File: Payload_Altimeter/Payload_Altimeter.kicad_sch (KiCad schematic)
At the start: 0 parts

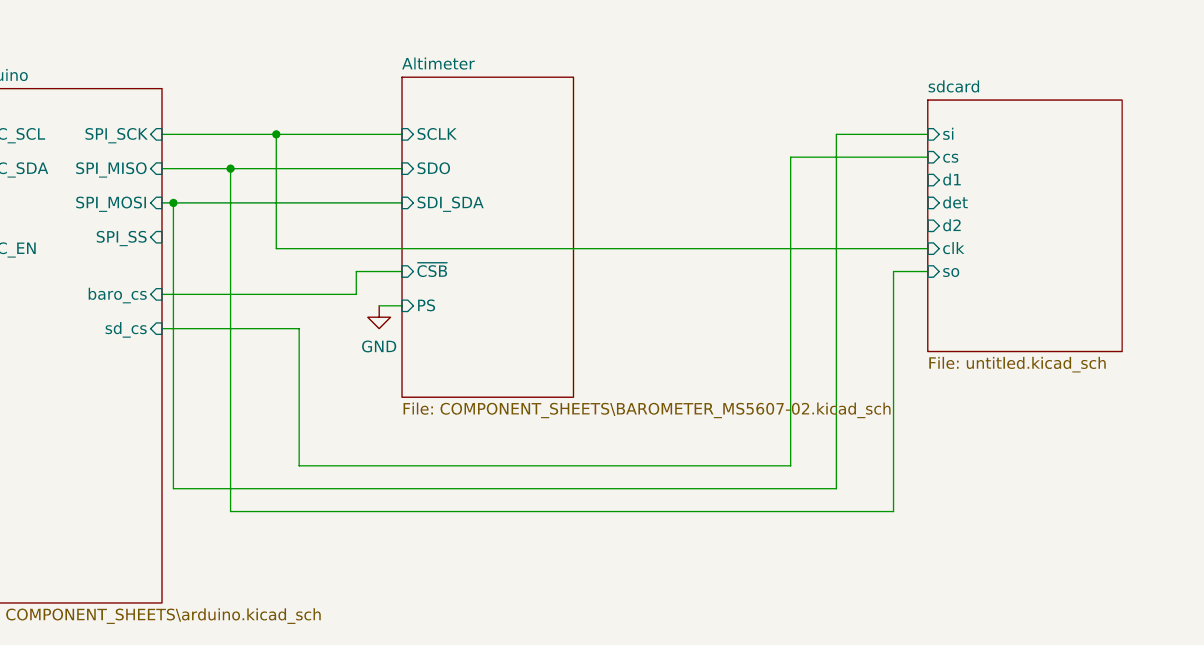
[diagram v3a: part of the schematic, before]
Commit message: SD Card
Got rid of SD card
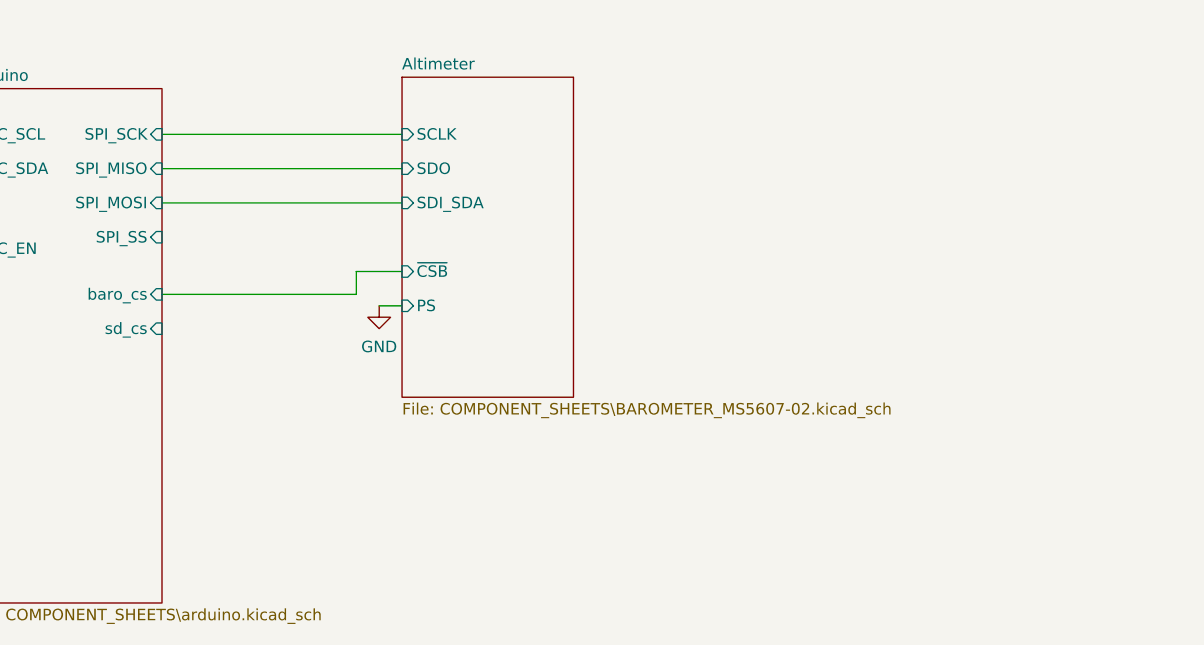
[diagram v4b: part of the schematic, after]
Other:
- removed sheet sdcard
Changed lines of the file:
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@@
 (kicad_sch (version 20211123) (generator eeschema)
   (paper "A4")
-  (junction (at 134.62 71.12) (diameter 0) (color 0 0 0 0)
-  )
-  (junction (at 129.54 74.93) (diameter 0) (color 0 0 0 0)
-  )
-  (junction (at 123.19 78.74) (diameter 0) (color 0 0 0 0)
-  )
-  (wire (pts (xy 134.62 71.12) (xy 148.59 71.12))
-    (stroke (width 0) (type default) (color 0 0 0 0))
-  )
   (wire (pts (xy 66.04 71.12) (xy 100.33 71.12))
     (stroke (width 0) (type default) (color 0 0 0 0))
   )
-  (wire (pts (xy 191.77 107.95) (xy 191.77 73.66))
-    (stroke (width 0) (type default) (color 0 0 0 0))
-  )
-  (wire (pts (xy 196.85 110.49) (xy 196.85 71.12))
-    (stroke (width 0) (type default) (color 0 0 0 0))
-  )
   (wire (pts (xy 143.51 86.36) (xy 148.59 86.36))
     (stroke (width 0) (type default) (color 0 0 0 0))
   )
-  (wire (pts (xy 134.62 83.82) (xy 134.62 71.12))
-    (stroke (width 0) (type default) (color 0 0 0 0))
-  )
-  (wire (pts (xy 123.19 110.49) (xy 196.85 110.49))
-    (stroke (width 0) (type default) (color 0 0 0 0))
-  )
-  (wire (pts (xy 123.19 78.74) (xy 123.19 110.49))
-    (stroke (width 0) (type default) (color 0 0 0 0))
-  )
   (wire (pts (xy 121.92 88.9) (xy 143.51 88.9))
     (stroke (width 0) (type default) (color 0 0 0 0))
   )
-  (wire (pts (xy 129.54 74.93) (xy 148.59 74.93))
-    (stroke (width 0) (type default) (color 0 0 0 0))
-  )
-  (wire (pts (xy 207.01 86.36) (xy 203.2 86.36))
-    (stroke (width 0) (type default) (color 0 0 0 0))
-  )
-  (wire (pts (xy 121.92 92.71) (xy 137.16 92.71))
-    (stroke (width 0) (type default) (color 0 0 0 0))
-  )
-  (wire (pts (xy 123.19 78.74) (xy 148.59 78.74))
+  (wire (pts (xy 121.92 78.74) (xy 148.59 78.74))
     (stroke (width 0) (type default) (color 0 0 0 0))
   )
@@
     (stroke (width 0) (type default) (color 0 0 0 0))
   )
-  (wire (pts (xy 196.85 71.12) (xy 207.01 71.12))
-    (stroke (width 0) (type default) (color 0 0 0 0))
-  )
   (wire (pts (xy 143.51 88.9) (xy 143.51 86.36))
     (stroke (width 0) (type default) (color 0 0 0 0))
   )
-  (wire (pts (xy 121.92 78.74) (xy 123.19 78.74))
-    (stroke (width 0) (type default) (color 0 0 0 0))
-  )
-  (wire (pts (xy 203.2 113.03) (xy 129.54 113.03))
-    (stroke (width 0) (type default) (color 0 0 0 0))
-  )
-  (wire (pts (xy 129.54 113.03) (xy 129.54 74.93))
-    (stroke (width 0) (type default) (color 0 0 0 0))
-  )
   (wire (pts (xy 146.05 90.17) (xy 148.59 90.17))
     (stroke (width 0) (type default) (color 0 0 0 0))
   )
-  (wire (pts (xy 137.16 92.71) (xy 137.16 107.95))
-    (stroke (width 0) (type default) (color 0 0 0 0))
-  )
-  (wire (pts (xy 137.16 107.95) (xy 191.77 107.95))
-    (stroke (width 0) (type default) (color 0 0 0 0))
-  )
-  (wire (pts (xy 191.77 73.66) (xy 207.01 73.66))
-    (stroke (width 0) (type default) (color 0 0 0 0))
-  )
-  (wire (pts (xy 207.01 83.82) (xy 134.62 83.82))
-    (stroke (width 0) (type default) (color 0 0 0 0))
-  )
-  (wire (pts (xy 121.92 74.93) (xy 129.54 74.93))
+  (wire (pts (xy 121.92 74.93) (xy 148.59 74.93))
     (stroke (width 0) (type default) (color 0 0 0 0))
   )
@@
     (stroke (width 0) (type default) (color 0 0 0 0))
   )
-  (wire (pts (xy 121.92 71.12) (xy 134.62 71.12))
-    (stroke (width 0) (type default) (color 0 0 0 0))
-  )
-  (wire (pts (xy 203.2 86.36) (xy 203.2 113.03))
+  (wire (pts (xy 121.92 71.12) (xy 148.59 71.12))
     (stroke (width 0) (type default) (color 0 0 0 0))
   )
@@
     )
   )
-  (sheet (at 207.01 67.31) (size 21.59 27.94) (fields_autoplaced)
-    (stroke (width 0.1524) (type solid) (color 0 0 0 0))
-    (fill (color 0 0 0 0.0000))
-    (property "Sheet name" "sdcard" (id 0) (at 207.01 66.5984 0)
-      (effects (font (size 1.27 1.27)) (justify left bottom))
-    )
-    (property "Sheet file" "untitled.kicad_sch" (id 1) (at 207.01 95.8346 0)
-      (effects (font (size 1.27 1.27)) (justify left top))
-    )
-    (pin "si" input (at 207.01 71.12 180)
-      (effects (font (size 1.27 1.27)) (justify left))
-    )
-    (pin "cs" input (at 207.01 73.66 180)
-      (effects (font (size 1.27 1.27)) (justify left))
-    )
-    (pin "d1" input (at 207.01 76.2 180)
-      (effects (font (size 1.27 1.27)) (justify left))
-    )
-    (pin "det" input (at 207.01 78.74 180)
-      (effects (font (size 1.27 1.27)) (justify left))
-    )
-    (pin "d2" input (at 207.01 81.28 180)
-      (effects (font (size 1.27 1.27)) (justify left))
-    )
-    (pin "clk" input (at 207.01 83.82 180)
-      (effects (font (size 1.27 1.27)) (justify left))
-    )
-    (pin "so" input (at 207.01 86.36 180)
-      (effects (font (size 1.27 1.27)) (justify left))
-    )
-  )
   (sheet_instances
     (path "/" (page "1"))
@@
     (path "/5fba5415-62df-4f11-b066-c862c7f4f614" (page "3"))
     (path "/18be7ca6-5942-4bc1-bf13-c4393b1dbad1" (page "4"))
-    (path "/abdb6179-bbd9-4d88-83fc-0a11cdff4490" (page "5"))
   )
   (symbol_instances
@@
       (reference "#PWR0105") (unit 1) (value "+5V") (footprint "")
     )
-    (path "/abdb6179-bbd9-4d88-83fc-0a11cdff4490/b48e6861-adf2-4473-858f-d65f8dcea6c9"
-      (reference "#PWR0106") (unit 1) (value "+3V3") (footprint "")
-    )
-    (path "/abdb6179-bbd9-4d88-83fc-0a11cdff4490/d5954016-c980-4371-a52c-a53007d822f3"
-      (reference "#PWR0107") (unit 1) (value "GND") (footprint "")
-    )
     (path "/5fba5415-62df-4f11-b066-c862c7f4f614/00000000-0000-0000-0000-000061610282"
       (reference "C12") (unit 1) (value "100nF") (footprint "Capacitor_SMD:C_0201_0603Metric")
@@
       (reference "J1") (unit 1) (value "L717SDC37P1ACH4F") (footprint "RDT_Custom_Footprints:L717SDC37P1ACH4F")
     )
-    (path "/abdb6179-bbd9-4d88-83fc-0a11cdff4490/71d6f518-fb46-4753-adea-d4368d3f3e26"
-      (reference "J2") (unit 1) (value "Conn_01x09") (footprint "Connector_PinHeader_2.54mm:PinHeader_1x09_P2.54mm_Vertical")
-    )
     (path "/18be7ca6-5942-4bc1-bf13-c4393b1dbad1/4ac59da2-094a-4712-84ed-13816bdf2b3f"

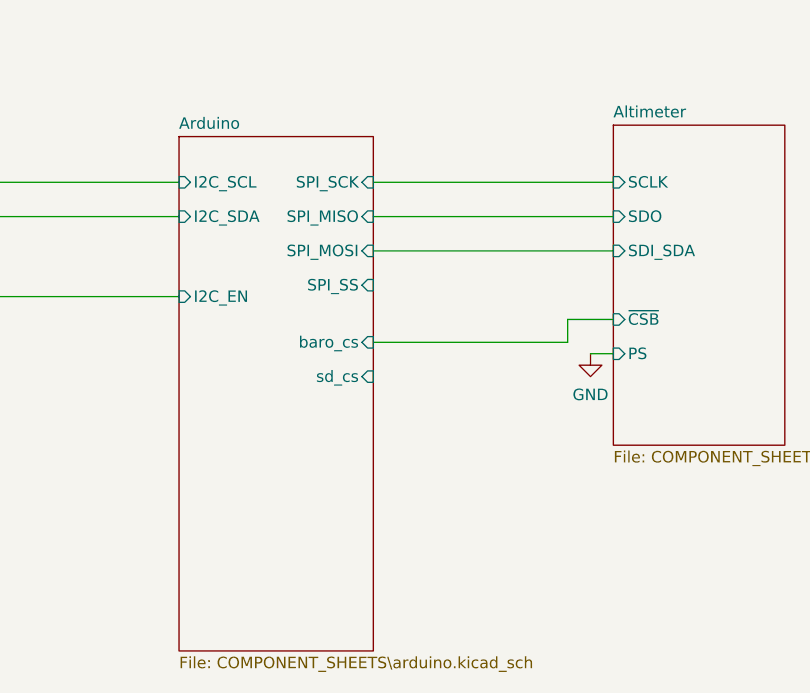
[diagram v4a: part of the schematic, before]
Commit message: Rasp_Pi
Tried to put in a pi zero
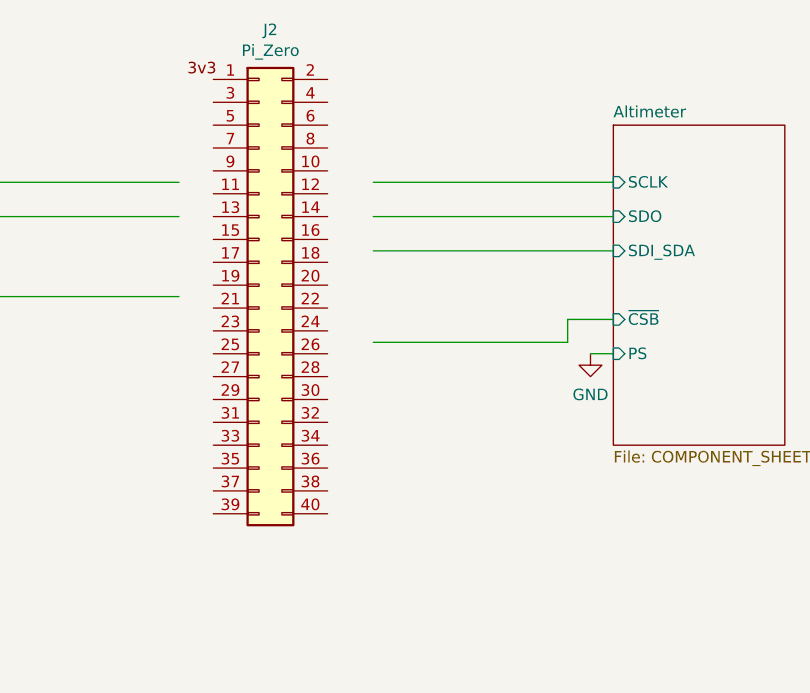
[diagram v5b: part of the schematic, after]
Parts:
- added J2: Pi_Zero, Connector_PinHeader_2.54mm:PinHeader_2x20_P2.54mm_Vertical, symbol Connector_Generic:Conn_02x20_Odd_Even
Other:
- removed sheet Arduino
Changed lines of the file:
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@@
     (stroke (width 0) (type default) (color 0 0 0 0))
+  )
+  (symbol (lib_id "Connector_Generic:Conn_02x20_Odd_Even") (at 109.22 82.55 0) (unit 1)
+    (in_bom yes) (on_board yes)
+    (property "Reference" "J2" (id 0) (at 110.49 54.1782 0))
+    (property "Value" "Pi_Zero" (id 1) (at 110.49 56.4896 0))
+    (property "Footprint" "Connector_PinHeader_2.54mm:PinHeader_2x20_P2.54mm_Vertical" (id 2) (at 109.22 82.55 0)
+      (effects (font (size 1.27 1.27)) hide)
+    )
+    (property "Datasheet" "~" (id 3) (at 109.22 82.55 0)
+      (effects (font (size 1.27 1.27)) hide)
+    )
+    (pin "1")
+    (pin "10")
+    (pin "11")
+    (pin "12")
+    (pin "13")
+    (pin "14")
+    (pin "15")
+    (pin "16")
+    (pin "17")
+    (pin "18")
+    (pin "19")
+    (pin "2")
+    (pin "20")
+    (pin "21")
+    (pin "22")
+    (pin "23")
+    (pin "24")
+    (pin "25")
+    (pin "26")
+    (pin "27")
+    (pin "28")
+    (pin "29")
+    (pin "3")
+    (pin "30")
+    (pin "31")
+    (pin "32")
+    (pin "33")
+    (pin "34")
+    (pin "35")
+    (pin "36")
+    (pin "37")
+    (pin "38")
+    (pin "39")
+    (pin "4")
+    (pin "40")
+    (pin "5")
+    (pin "6")
+    (pin "7")
+    (pin "8")
+    (pin "9")
   )
   (symbol (lib_id "power:GND") (at 146.05 90.17 0) (unit 1)
@@
     )
   )
-  (sheet (at 100.33 66.04) (size 21.59 57.15) (fields_autoplaced)
-    (stroke (width 0.1524) (type solid) (color 0 0 0 0))
-    (fill (color 0 0 0 0.0000))
-    (property "Sheet name" "Arduino" (id 0) (at 100.33 65.3284 0)
-      (effects (font (size 1.27 1.27)) (justify left bottom))
-    )
-    (property "Sheet file" "COMPONENT_SHEETS\\arduino.kicad_sch" (id 1) (at 100.33 123.7746 0)
-      (effects (font (size 1.27 1.27)) (justify left top))
-    )
-    (pin "I2C_SCL" input (at 100.33 71.12 180)
-      (effects (font (size 1.27 1.27)) (justify left))
-    )
-    (pin "I2C_SDA" input (at 100.33 74.93 180)
-      (effects (font (size 1.27 1.27)) (justify left))
-    )
-    (pin "I2C_EN" input (at 100.33 83.82 180)
-      (effects (font (size 1.27 1.27)) (justify left))
-    )
-    (pin "SPI_SCK" input (at 121.92 71.12 0)
-      (effects (font (size 1.27 1.27)) (justify right))
-    )
-    (pin "SPI_MISO" input (at 121.92 74.93 0)
-      (effects (font (size 1.27 1.27)) (justify right))
-    )
-    (pin "SPI_MOSI" input (at 121.92 78.74 0)
-      (effects (font (size 1.27 1.27)) (justify right))
-    )
-    (pin "SPI_SS" input (at 121.92 82.55 0)
-      (effects (font (size 1.27 1.27)) (justify right))
-    )
-    (pin "baro_cs" input (at 121.92 88.9 0)
-      (effects (font (size 1.27 1.27)) (justify right))
-    )
-    (pin "sd_cs" input (at 121.92 92.71 0)
-      (effects (font (size 1.27 1.27)) (justify right))
-    )
-  )
   (sheet (at 148.59 64.77) (size 19.05 35.56) (fields_autoplaced)
     (stroke (width 0.1524) (type solid) (color 0 0 0 0))
@@
     (path "/0730ce47-0bea-44a3-992c-5d03f0a08e83" (page "2"))
     (path "/5fba5415-62df-4f11-b066-c862c7f4f614" (page "3"))
-    (path "/18be7ca6-5942-4bc1-bf13-c4393b1dbad1" (page "4"))
   )
   (symbol_instances
@@
       (reference "#PWR0101") (unit 1) (value "GND") (footprint "")
     )
-    (path "/18be7ca6-5942-4bc1-bf13-c4393b1dbad1/98b5fd41-6856-4d34-bc02-2d1bbe8972be"
-      (reference "#PWR0102") (unit 1) (value "+5V") (footprint "")
-    )
-    (path "/18be7ca6-5942-4bc1-bf13-c4393b1dbad1/44276706-5572-4ca8-88fc-56e6f30954a6"
-      (reference "#PWR0103") (unit 1) (value "GND") (footprint "")
-    )
     (path "/0730ce47-0bea-44a3-992c-5d03f0a08e83/58442b5d-6983-40cc-bc9c-d8f0af4d6d86"
       (reference "#PWR0104") (unit 1) (value "+5V") (footprint "")
@@
       (reference "J1") (unit 1) (value "L717SDC37P1ACH4F") (footprint "RDT_Custom_Footprints:L717SDC37P1ACH4F")
     )
-    (path "/18be7ca6-5942-4bc1-bf13-c4393b1dbad1/4ac59da2-094a-4712-84ed-13816bdf2b3f"
-      (reference "U1") (unit 1) (value "Arduino_Pro_Mini") (footprint "Arduino:Arduino_Pro_Mini")
+    (path "/3c366a71-f7c8-4705-a28c-1a6b708315a6"
+      (reference "J2") (unit 1) (value "Pi_Zero") (footprint "Connector_PinHeader_2.54mm:PinHeader_2x20_P2.54mm_Vertical")
     )
     (path "/5fba5415-62df-4f11-b066-c862c7f4f614/00000000-0000-0000-0000-00006161026e"

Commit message: Finished Schematic?
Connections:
- net Pi_3v3: now reaches J2.1 (3v3)
- net MOSI: now reaches J2.19 (Pin_19)
- net +5V: now reaches J2.2 (Pin_2)
- net +5V: now also J2.4 (Pin_4)
- net MISO: now reaches J2.21 (Pin_21)
- net SCLK: now reaches J2.23 (Pin_23)
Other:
- sheet Altimeter renamed Barometer
- sheet Barometer ports: added 3v3, MISO, MOSI; removed PS, SDI_SDA, SDO, ~{CSB}

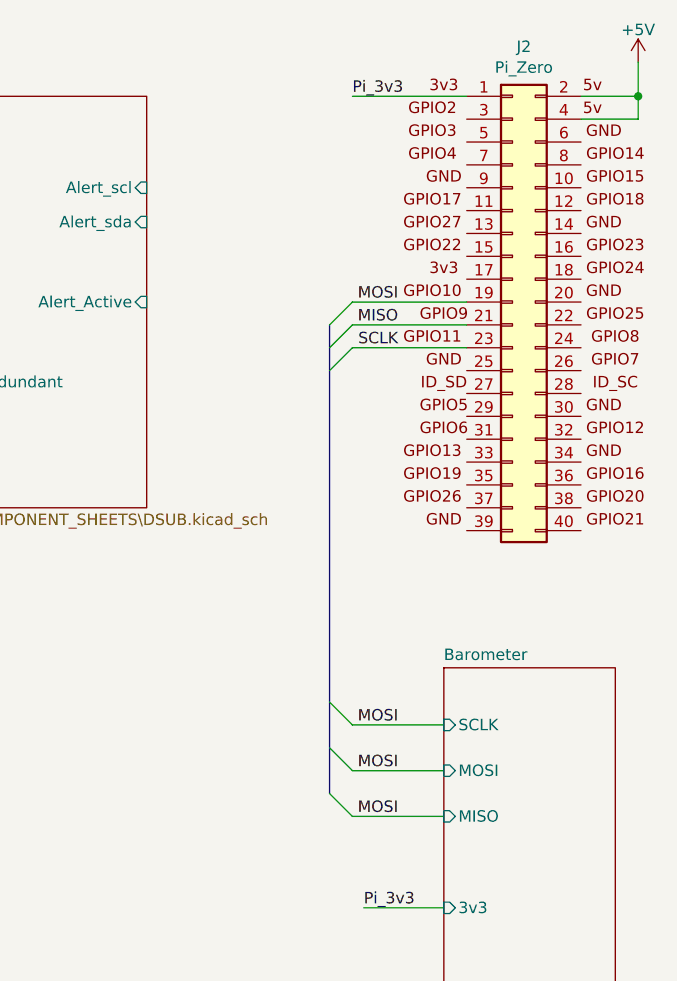
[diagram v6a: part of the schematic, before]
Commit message: Some connection
Put some of the connections on but not all of them
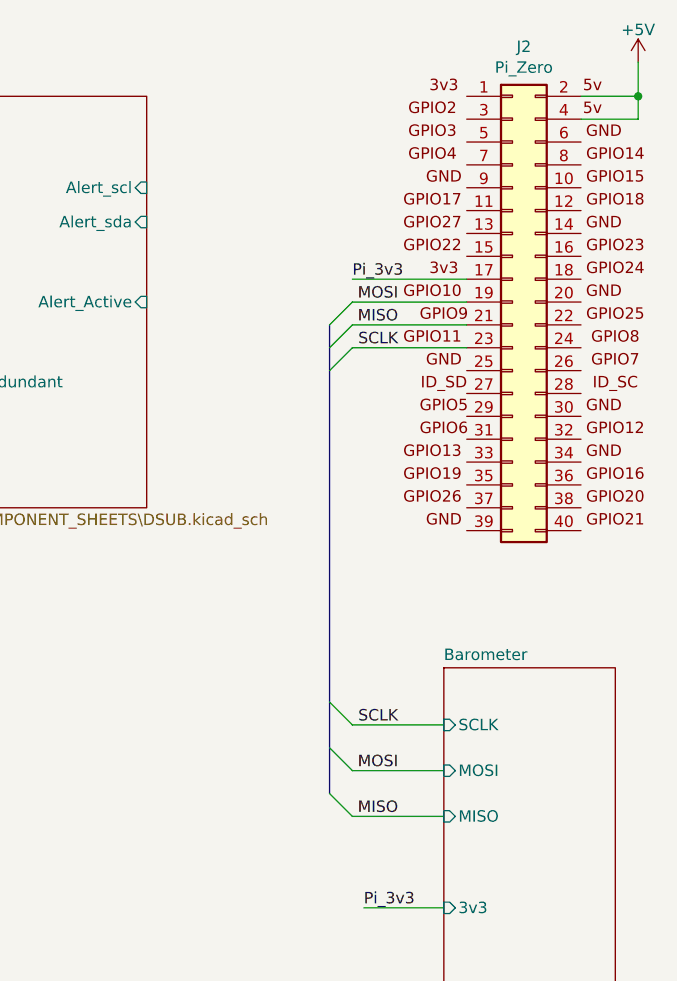
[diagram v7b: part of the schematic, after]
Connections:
- net Pi_3v3: now also J2.17 (Pin_17); no longer J2.1 (3v3)
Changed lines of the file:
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@@
+    (stroke (width 0) (type default) (color 0 0 0 0))
+  )
+  (wire (pts (xy 81.28 59.69) (xy 93.98 59.69))
     (stroke (width 0) (type default) (color 0 0 0 0))
   )
@@
     (stroke (width 0) (type default) (color 0 0 0 0))
   )
-  (wire (pts (xy 81.28 39.37) (xy 93.98 39.37))
-    (stroke (width 0) (type default) (color 0 0 0 0))
-  )
   (wire (pts (xy 106.68 39.37) (xy 113.03 39.37))
     (stroke (width 0) (type default) (color 0 0 0 0))
@@
   (wire (pts (xy 81.28 114.3) (xy 91.44 114.3))
     (stroke (width 0) (type default) (color 0 0 0 0))
+  )
+  (label "SCLK" (at 86.36 109.22 180)
+    (effects (font (size 1.27 1.27)) (justify right bottom))
   )
   (label "Pi_3v3" (at 82.55 129.54 0)
     (effects (font (size 1.27 1.27)) (justify left bottom))
   )
-  (label "MOSI" (at 86.36 119.38 180)
-    (effects (font (size 1.27 1.27)) (justify right bottom))
-  )
   (label "SCLK" (at 86.36 67.31 180)
     (effects (font (size 1.27 1.27)) (justify right bottom))
@@
     (effects (font (size 1.27 1.27)) (justify right bottom))
   )
-  (label "Pi_3v3" (at 81.28 39.37 0)
+  (label "MISO" (at 86.36 119.38 180)
+    (effects (font (size 1.27 1.27)) (justify right bottom))
+  )
+  (label "Pi_3v3" (at 81.28 59.69 0)
     (effects (font (size 1.27 1.27)) (justify left bottom))
   )
   (label "MISO" (at 86.36 64.77 180)
-    (effects (font (size 1.27 1.27)) (justify right bottom))
-  )
-  (label "MOSI" (at 86.36 109.22 180)
     (effects (font (size 1.27 1.27)) (justify right bottom))
   )
   (symbol (lib_id "power:+5V") (at 113.03 35.56 0) (unit 1)
     (in_bom yes) (on_board yes) (fields_autoplaced)
-    (property "Reference" "#PWR?" (id 0) (at 113.03 39.37 0)
+    (property "Reference" "#PWR0101" (id 0) (at 113.03 39.37 0)
       (effects (font (size 1.27 1.27)) hide)
     )
@@
       (reference "#PWR040") (unit 1) (value "GND") (footprint "")
     )
+    (path "/218e0fc5-0855-49a5-b991-b2ea0e27f644"
+      (reference "#PWR0101") (unit 1) (value "+5V") (footprint "")
+    )
     (path "/0730ce47-0bea-44a3-992c-5d03f0a08e83/58442b5d-6983-40cc-bc9c-d8f0af4d6d86"
       (reference "#PWR0104") (unit 1) (value "+5V") (footprint "")
@@
       (reference "#PWR0105") (unit 1) (value "+5V") (footprint "")
     )
-    (path "/218e0fc5-0855-49a5-b991-b2ea0e27f644"
-      (reference "#PWR?") (unit 1) (value "+5V") (footprint "")
-    )
     (path "/5fba5415-62df-4f11-b066-c862c7f4f614/00000000-0000-0000-0000-000061610282"

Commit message: Finished PCB Layout
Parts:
- added TP1: Pi_3v3, TestPoint:TestPoint_Pad_D2.0mm, symbol Connector:TestPoint
- added TP2: 5V, TestPoint:TestPoint_Pad_D2.0mm, symbol Connector:TestPoint
- added TP3: SCLK, TestPoint:TestPoint_Pad_D2.0mm, symbol Connector:TestPoint
- added TP4: MOSI, TestPoint:TestPoint_Pad_D2.0mm, symbol Connector:TestPoint
- added TP5: MISO, TestPoint:TestPoint_Pad_D2.0mm, symbol Connector:TestPoint
- added TP6: GND, TestPoint:TestPoint_Pad_D2.0mm, symbol Connector:TestPoint
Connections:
- net +5V: now also TP2.1
- net MISO: now also TP5.1
- net MOSI: now also TP4.1
- net Pi_3v3: now also TP1.1
- net SCLK: now also TP3.1
- net GND: now reaches J2.14 (Pin_14)
- net GND: now also J2.20 (Pin_20), J2.25 (Pin_25), J2.30 (Pin_30), J2.34 (Pin_34), J2.39 (Pin_39), J2.6 (Pin_6), J2.9 (Pin_9), TP6.1
